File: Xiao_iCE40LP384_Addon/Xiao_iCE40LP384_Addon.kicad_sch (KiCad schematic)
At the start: 26 parts, among them J1 Conn_01x07_Pin, J2 Conn_01x07_Pin, SW1 SW_Push, U1 ICE40LP384-SG32, U2 ADP322ACPZ-145-R7, U4 XIAO-SAMD21-SMD

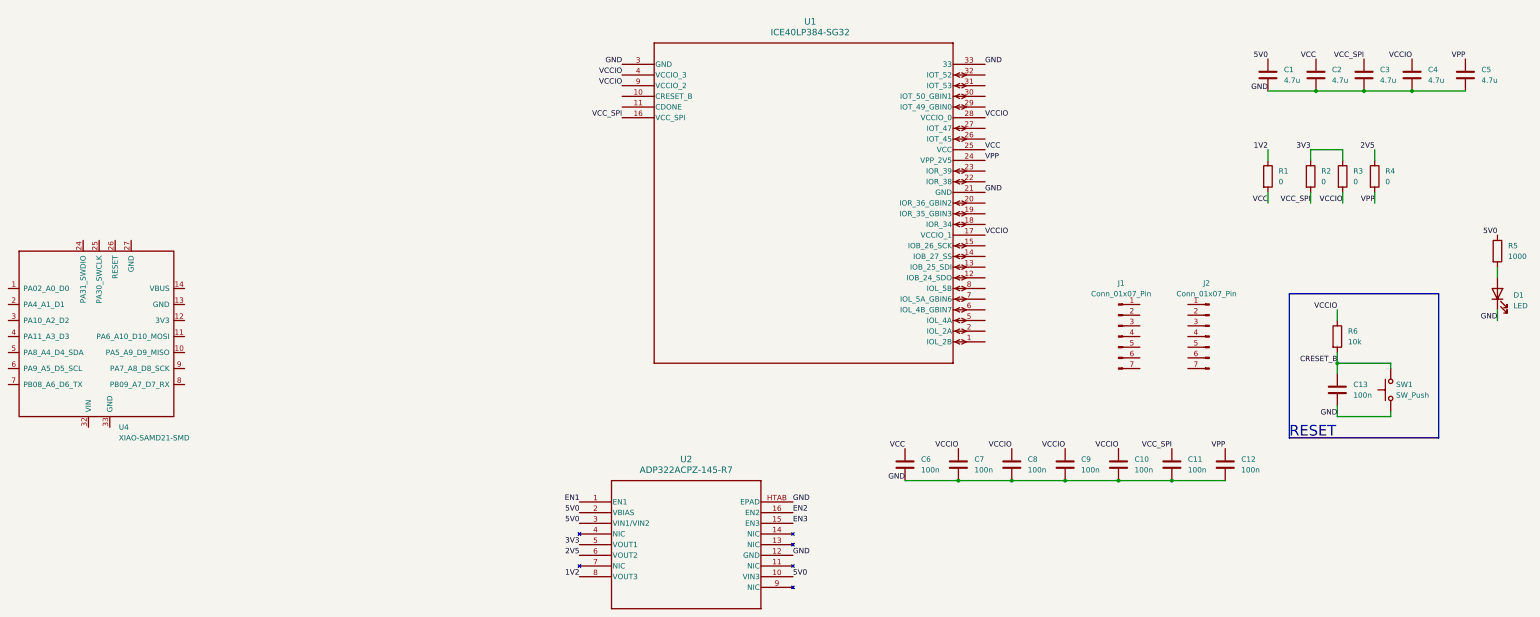
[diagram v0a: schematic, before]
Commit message: Finished most of the XIAO floorplan, need to route FPGA caps
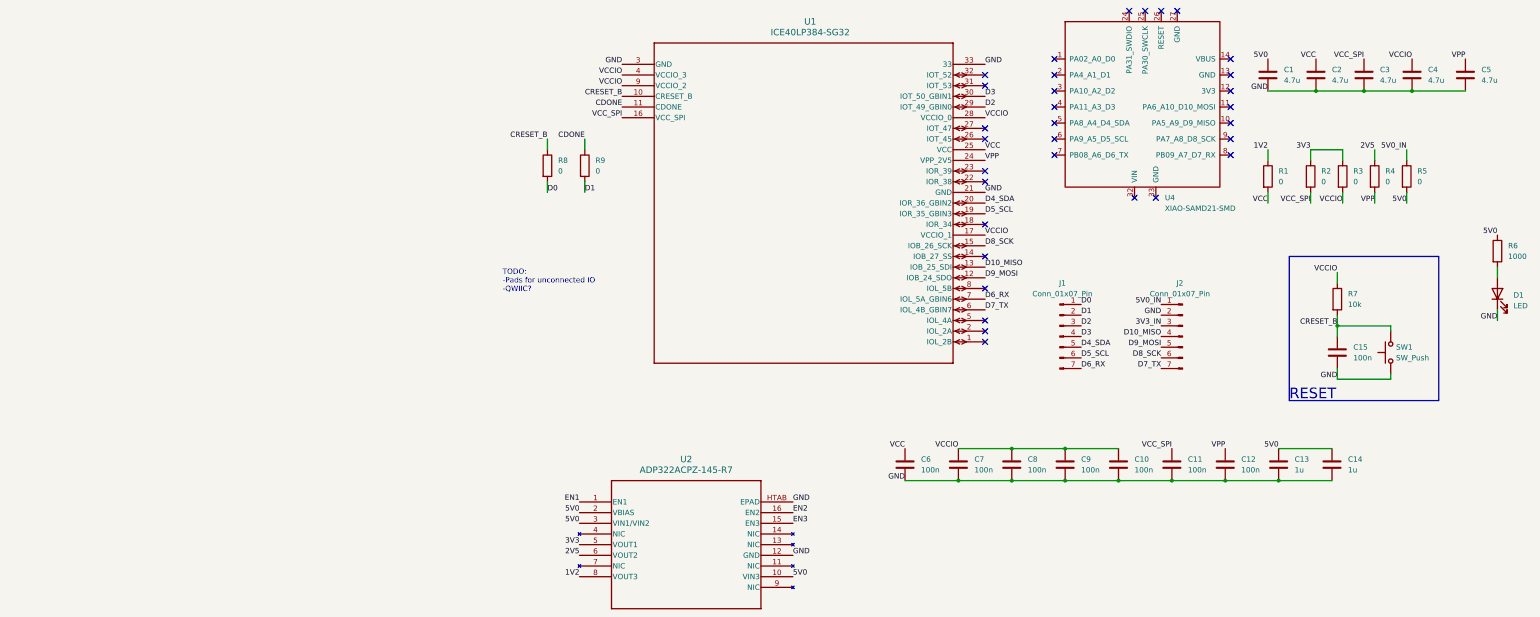
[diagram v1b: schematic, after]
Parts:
- added C13, C14: 1u, Capacitor_SMD:C_0402_1005Metric, symbol Device:C
- added R5, R8, R9: 0, Resistor_SMD:R_0402_1005Metric, symbol Device:R
- C1, C10, C11, C12, C2, C3, C4, C5, C6, C7, C8, C9: footprint Capacitor_SMD:C_0603_1608Metric -> Capacitor_SMD:C_0402_1005Metric
- C15: renamed from C13; footprint Capacitor_SMD:C_0603_1608Metric -> Capacitor_SMD:C_0402_1005Metric
- D1: footprint LED_SMD:LED_0603_1608Metric -> LED_SMD:LED_0402_1005Metric
- R1, R2, R3, R4: footprint Resistor_SMD:R_0603_1608Metric -> Resistor_SMD:R_0402_1005Metric
- R6: renamed from R5; footprint Resistor_SMD:R_0603_1608Metric -> Resistor_SMD:R_0402_1005Metric
- R7: renamed from R6; footprint Resistor_SMD:R_0603_1608Metric -> Resistor_SMD:R_0402_1005Metric
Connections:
- net 5V0: now also C13.1, C14.1, R5.2
- net CRESET_B: now also U1.10 (CRESET_B), R8.1
- net GND: now also J2.2 (Pin_2), C13.2, C14.2
- net 5V0_IN: now reaches J2.1 (Pin_1)
- net 5V0_IN: now also R5.1
- net 3V3_IN: now reaches J2.3 (Pin_3)
- net D10_MISO: now reaches J2.4 (Pin_4)
- net D10_MISO: now also U1.13 (IOB_25_SDI)
- net D9_MOSI: now reaches J2.5 (Pin_5)
- net D9_MOSI: now also U1.12 (IOB_24_SDO)
- net D8_SCK: now reaches J2.6 (Pin_6)
- net D8_SCK: now also U1.15 (IOB_26_SCK)
- net D7_TX: now reaches J2.7 (Pin_7)
- net D7_TX: now also U1.6 (IOL_4B_GBIN7)
- net CDONE: now reaches U1.11 (CDONE)
- net CDONE: now also R9.1
- net D5_SCL: now reaches U1.19 (IOR_35_GBIN3)
- net D5_SCL: now also J1.6 (Pin_6)
- net D4_SDA: now reaches U1.20 (IOR_36_GBIN2)
- net D4_SDA: now also J1.5 (Pin_5)
- net D2: now reaches U1.29 (IOT_49_GBIN0)
- net D2: now also J1.3 (Pin_3)
- net D3: now reaches U1.30 (IOT_50_GBIN1)
- net D3: now also J1.4 (Pin_4)
- net D6_RX: now reaches U1.7 (IOL_5A_GBIN6)
- net D6_RX: now also J1.7 (Pin_7)
- net D0: now reaches J1.1 (Pin_1)
- net D0: now also R8.2
- net D1: now reaches J1.2 (Pin_2)
- net D1: now also R9.2
- no-connect marks 0 -> 32
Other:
- note added: "TODO: -Pads for unconnected IO -QWIIC?"
- moved on the sheet: C15, J1, J2, R7, SW1, U4

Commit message: XIAO done, as long as no problems come up during prototype testing
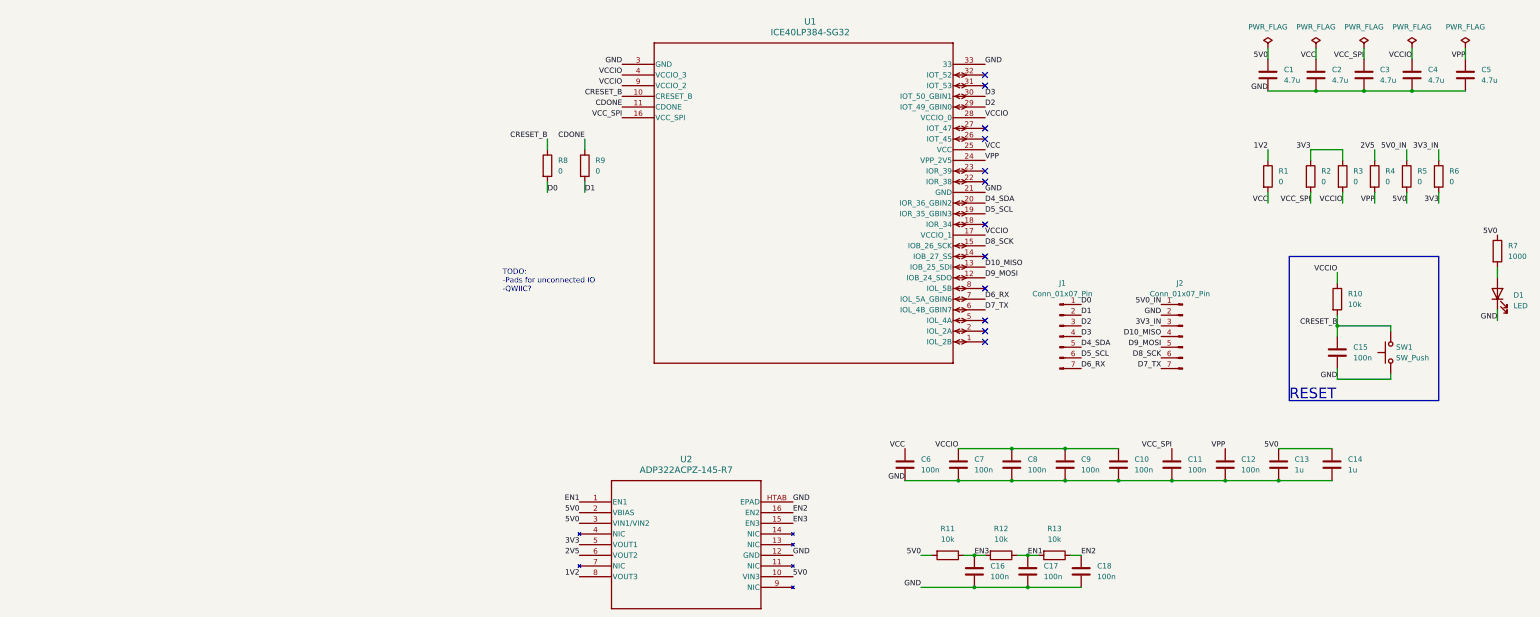
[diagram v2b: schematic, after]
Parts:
- removed U4: XIAO-SAMD21-SMD, XIAO Footprints and Symbols:XIAO-RP2040-SMD, symbol Seeed_Studio_XIAO_Series:XIAO-SAMD21-SMD
- added C16, C17, C18: 100n, Capacitor_SMD:C_0402_1005Metric, symbol Device:C
- added R11, R12, R13: 10k, Resistor_SMD:R_0402_1005Metric, symbol Device:R
- added R6: 0, Resistor_SMD:R_0402_1005Metric, symbol Device:R
- renumbered R7 to R10, R6 to R7
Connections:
- net 3V3: now also R6.2
- net 3V3_IN: now also R6.1
- net 5V0: now also R11.2
- net EN1: now also C17.1, R12.1, R13.2
- net EN2: now also C18.1, R13.1
- net EN3: now also C16.1, R11.1, R12.2
- net GND: now also C16.2, C17.2, C18.2
- no-connect marks 32 -> 12

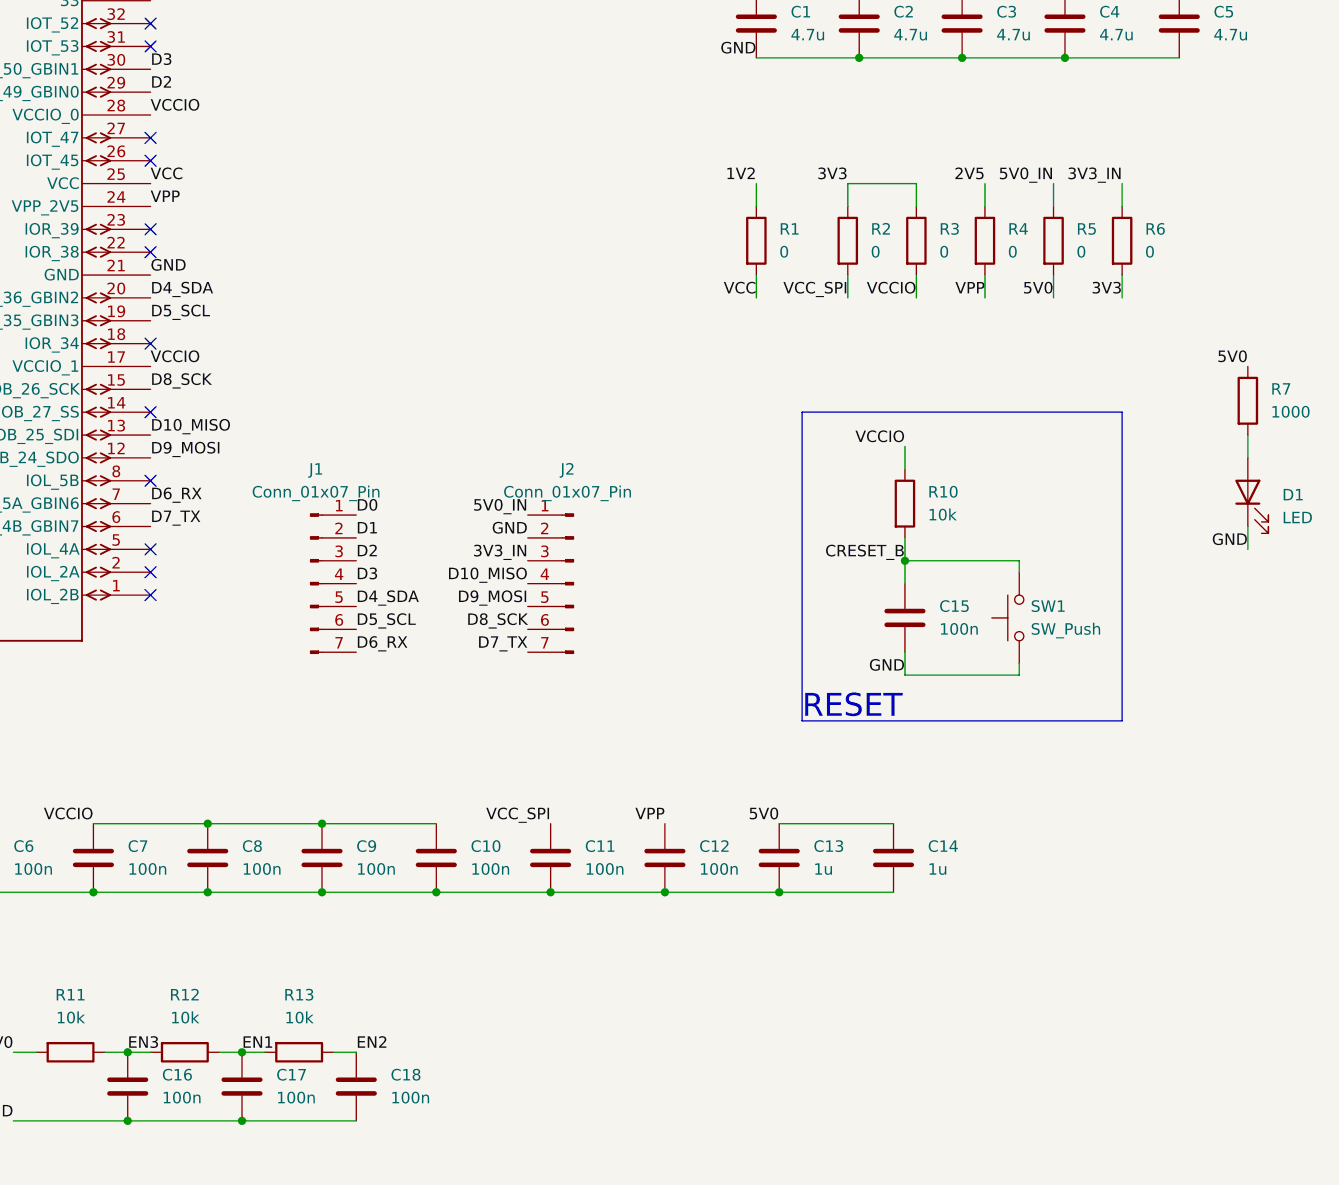
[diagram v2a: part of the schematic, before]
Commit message: Slow down RC timer and add test points to power supply
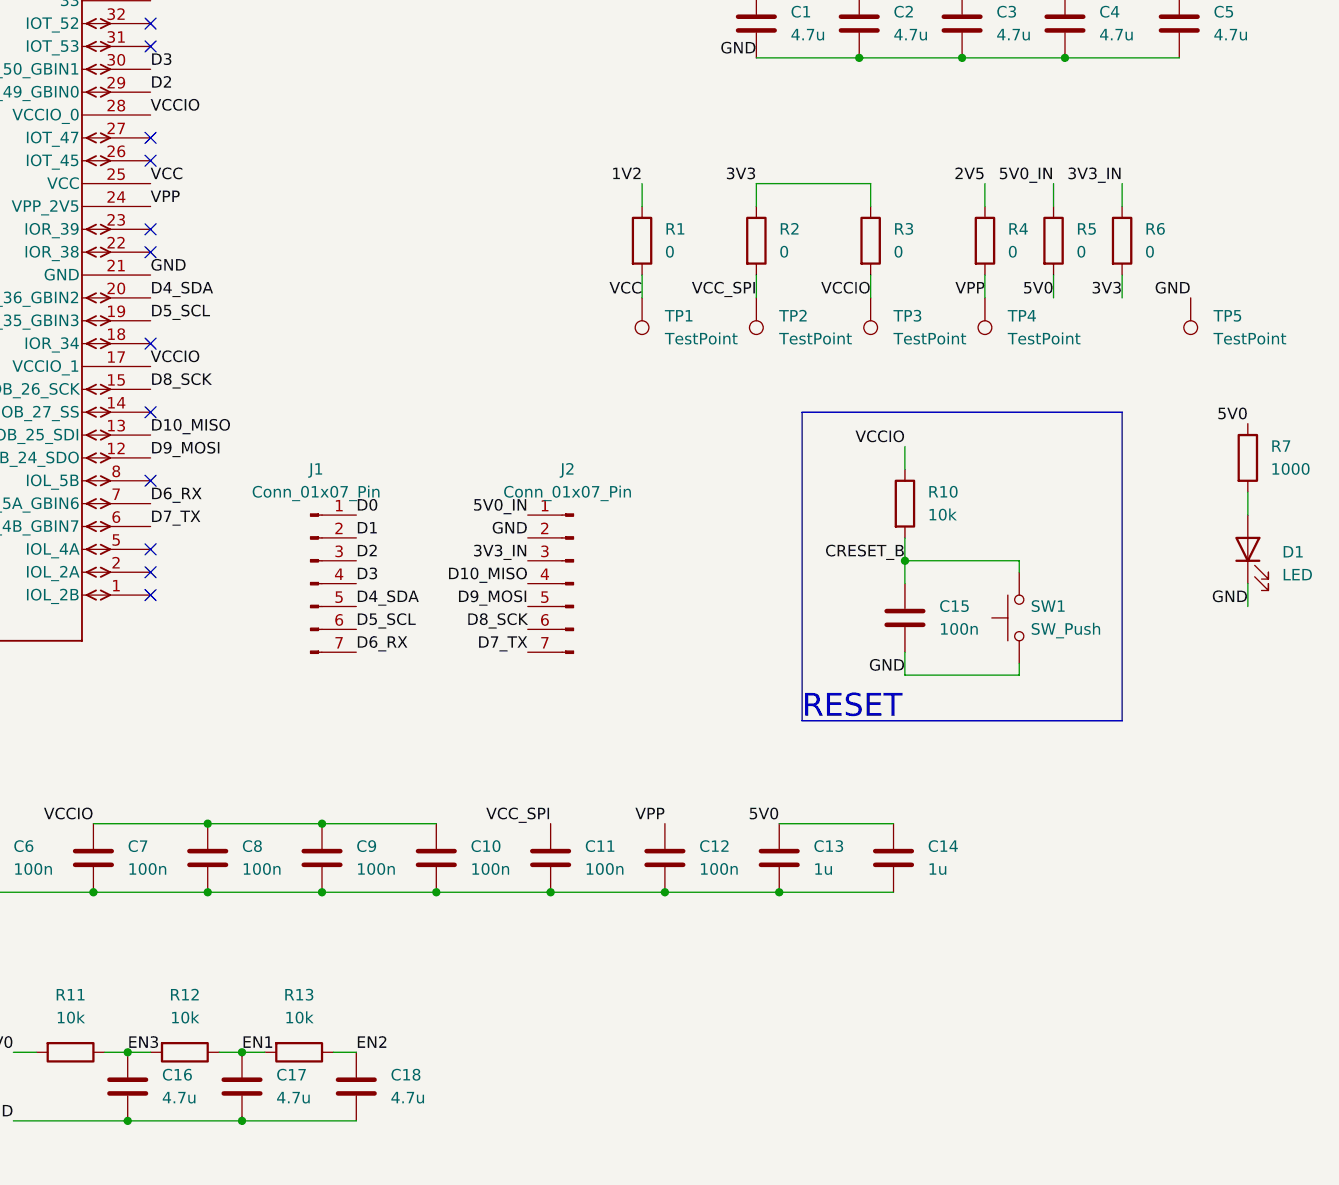
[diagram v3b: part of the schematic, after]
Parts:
- added TP1, TP2, TP3, TP4, TP5: TestPoint, TestPoint:TestPoint_Pad_1.0x1.0mm, symbol Connector:TestPoint
- C16, C17, C18: value 100n -> 4.7u
- D1: footprint LED_SMD:LED_0402_1005Metric -> LED_SMD:LED_0603_1608Metric
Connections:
- net GND: now also TP5.1
- net VCC: now also TP1.1
- net VCCIO: now also TP3.1
- net VCC_SPI: now also TP2.1
- net VPP: now also TP4.1
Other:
- moved on the sheet: D1, R1, R2, R3, R7
